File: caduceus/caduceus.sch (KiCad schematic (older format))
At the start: 47 parts

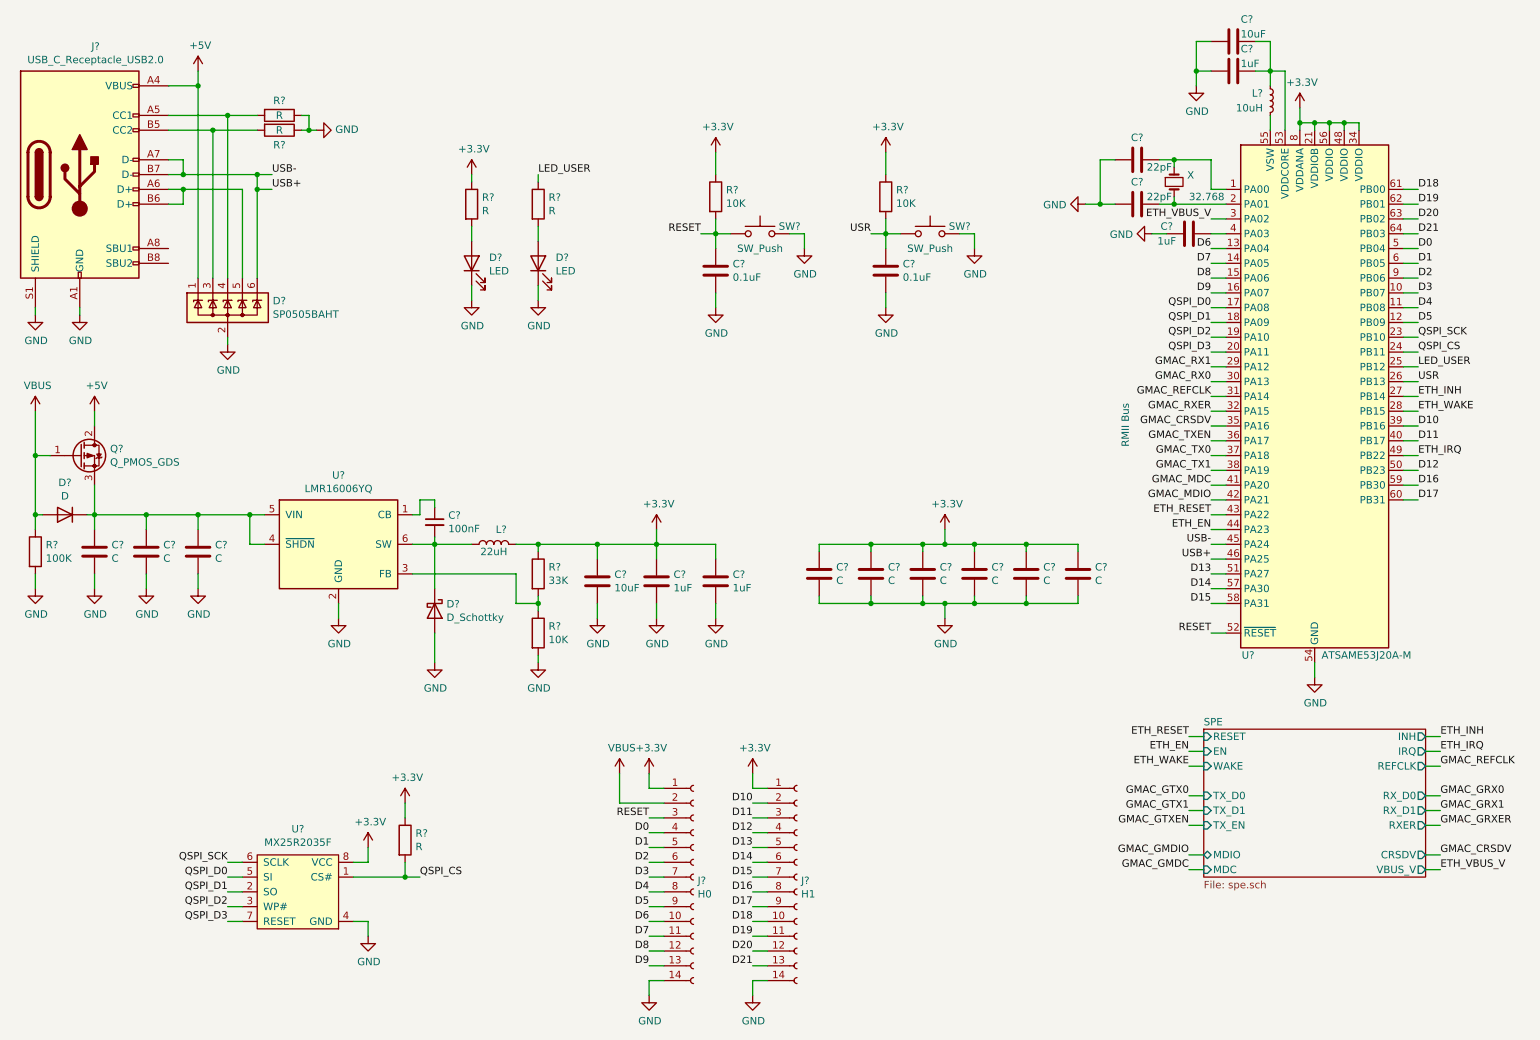
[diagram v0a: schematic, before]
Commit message: Footprints done, not all are final
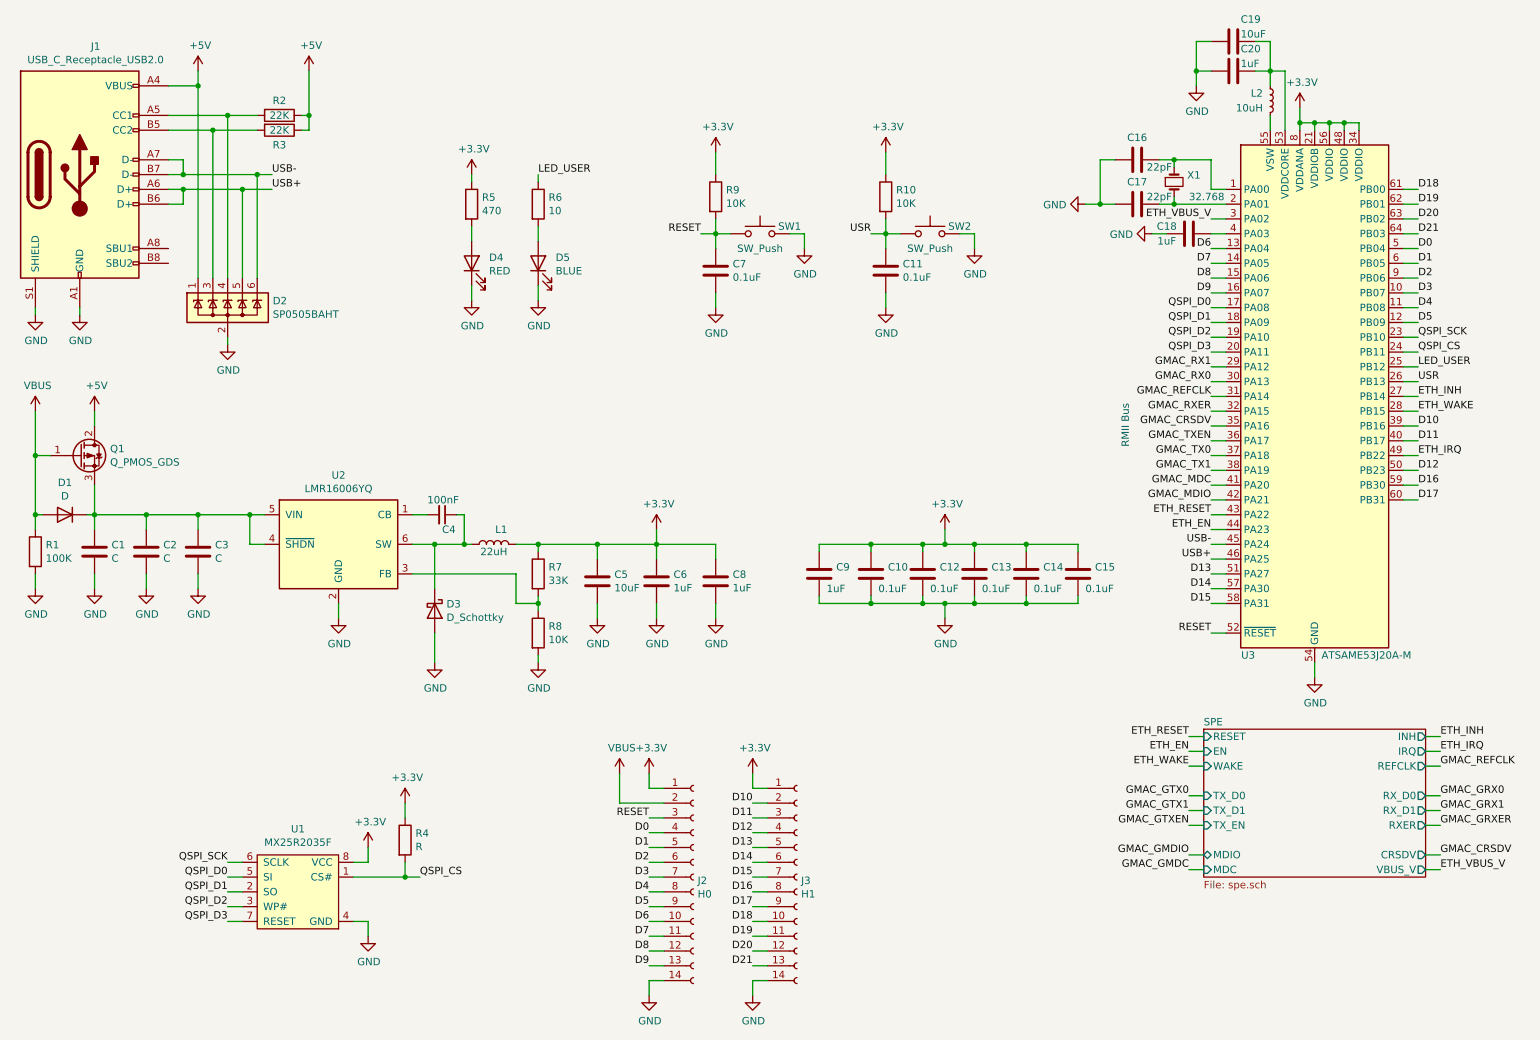
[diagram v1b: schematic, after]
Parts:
- C1, C11, C16, C17, C18, C19, C2, C20, C3, C4, C5, C6, C7, C8: renamed from C?; footprint (none) -> Capacitor_SMD:C_0603_1608Metric
- C10, C12, C13, C14, C15: renamed from C?; value C -> 0.1uF; footprint (none) -> Capacitor_SMD:C_0603_1608Metric
- C9: renamed from C?; value C -> 1uF; footprint (none) -> Capacitor_SMD:C_0603_1608Metric
- D4: renamed from D?; value LED -> RED; PN (none) -> LTST-C171KRKT
- D5: renamed from D?; value LED -> BLUE; PN (none) -> LTST-C171TBKT
- J1: renamed from J?; footprint (none) -> Connector_USB:USB_C_Receptacle_Amphenol_12401610E4-2A_CircularHoles
- J2: renamed from J?; footprint (none) -> Connector_PinHeader_2.54mm:PinHeader_1x10_P2.54mm_Vertical
- J3: renamed from J?; footprint (none) -> Button_Switch_SMD:SW_SPST_B3U-1000P
- R1, R10, R4, R7, R8, R9: renamed from R?; footprint (none) -> Resistor_SMD:R_0603_1608Metric
- R2, R3: renamed from R?; value R -> 22K; footprint (none) -> Resistor_SMD:R_0603_1608Metric
- R5: renamed from R?; value R -> 470; footprint (none) -> Resistor_SMD:R_0603_1608Metric
- R6: renamed from R?; value R -> 10; footprint (none) -> Resistor_SMD:R_0603_1608Metric
- SW1, SW2: renamed from SW?; footprint (none) -> Button_Switch_SMD:SW_SPST_B3U-1000P
- U1: renamed from U?; footprint (none) -> Package_SO:SOP-8_3.9x4.9mm_P1.27mm
- gave numbers to parts that had none: 8
- renumbered X to X1
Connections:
- net +5V: now also R2.1, R3.1
- net GND: no longer R2.1, R3.1
- net USB+: now also D2.5 (K), J1.A6 (D+), J1.B6 (D+); no longer D2.6 (K), J1.A7 (D-), J1.B7 (D-), U3.45 (PA24)
- net at D3.1 (K), L1.1, U2.6 (SW): now also C4.1; no longer C4.2
- net at U2.1 (CB): now also C4.2; no longer C4.1
- new net USB-: D2.6 (K), J1.A7 (D-), J1.B7 (D-), U3.45 (PA24)
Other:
- moved on the sheet: C4

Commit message: Changed PHY IC to DP83TD510E
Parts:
- D1, D3: footprint (none) -> Diode_SMD:D_SOD-123
- D4, D5: footprint (none) -> LED_SMD:LED_0805_2012Metric
- J2: footprint Connector_PinHeader_2.54mm:PinHeader_1x10_P2.54mm_Vertical -> Connector_PinHeader_2.54mm:PinHeader_1x14_P2.54mm_Vertical
- J3: footprint Button_Switch_SMD:SW_SPST_B3U-1000P -> Connector_PinHeader_2.54mm:PinHeader_1x14_P2.54mm_Vertical
- L1: footprint (none) -> Inductor_SMD:L_Coilcraft_XxL4020
- L2: footprint (none) -> Inductor_SMD:L_0805_2012Metric
- Q1: footprint (none) -> Package_TO_SOT_SMD:SOT-23
- SW2: footprint Button_Switch_SMD:SW_SPST_B3U-1000P -> Button_Switch_SMD:SW_SPST_B3U-1000P
- X1: footprint (none) -> Crystal:Crystal_SMD_TXC_9HT11-2Pin_2.0x1.2mm
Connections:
- net D0: now also J2.13 (Pin_13); no longer J2.4 (Pin_4)
- net D1: now also J2.12 (Pin_12); no longer J2.5 (Pin_5)
- net D2: now also J2.11 (Pin_11); no longer J2.6 (Pin_6)
- net D3: now also J2.10 (Pin_10); no longer J2.7 (Pin_7)
- net D4: now also J2.9 (Pin_9); no longer J2.8 (Pin_8)
- net D5: now also J2.8 (Pin_8); no longer J2.9 (Pin_9)
- net D6: now also J2.7 (Pin_7); no longer J2.10 (Pin_10)
- net D7: now also J2.6 (Pin_6); no longer J2.11 (Pin_11)
- net D8: now also J2.5 (Pin_5); no longer J2.12 (Pin_12)
- net D9: now also J2.4 (Pin_4); no longer J2.13 (Pin_13)
- net ETH_INH: no longer names the net of U3.27 (PB14)
- net GMAC_CRSDV renamed G_RDV
- net GMAC_MDC renamed G_MDC
- net GMAC_MDIO renamed G_MDIO
- net GMAC_REFCLK renamed G_REFCLK
- net GMAC_RX0 renamed G_RX0
- net GMAC_RX1 renamed G_RX1
- net GMAC_RXER renamed G_RXER
- net GMAC_TX0 renamed G_TX0
- net GMAC_TX1 renamed G_TX1
- net GMAC_TXEN renamed G_TXEN
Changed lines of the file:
@@
 F 0 "L2" H 9250 1200 50  0000 R CNN
 F 1 "10uH" H 9250 1100 50  0000 R CNN
-F 2 "" H 9300 1150 50  0001 C CNN
+F 2 "Inductor_SMD:L_0805_2012Metric" H 9300 1150 50  0001 C CNN
 F 3 "~" H 9300 1150 50  0001 C CNN
 	1    9300 1150
@@
 F 0 "X1" V 8604 1788 50  0000 L CNN
 F 1 "32.768" V 8750 1800 50  0000 L CNN
-F 2 "" H 8650 1700 50  0001 C CNN
+F 2 "Crystal:Crystal_SMD_TXC_9HT11-2Pin_2.0x1.2mm" H 8650 1700 50  0001 C CNN
 F 3 "~" H 8650 1700 50  0001 C CNN
 	1    8650 1700
@@
 $EndComp
 Text Label 8900 3750 2    50   ~ 0
-GMAC_MDC
+G_MDC
 Wire Wire Line
 	8900 2950 9000 2950
-Text Label 8900 2950 2    50   ~ 0
-GMAC_RX1
 Wire Wire Line
 	8900 3050 9000 3050
-Text Label 8900 3050 2    50   ~ 0
-GMAC_RX0
 Wire Wire Line
 	9000 3150 8900 3150
-Text Label 8900 3150 2    50   ~ 0
-GMAC_REFCLK
 Wire Wire Line
 	8900 3250 9000 3250
-Text Label 8900 3250 2    50   ~ 0
-GMAC_RXER
 Wire Wire Line
 	9000 3350 8900 3350
-Text Label 8900 3350 2    50   ~ 0
-GMAC_CRSDV
 Text Label 8900 3450 2    50   ~ 0
-GMAC_TXEN
+G_TXEN
 Wire Wire Line
 	8900 3450 9000 3450
@@
 	8900 3550 9000 3550
 Text Label 8900 3550 2    50   ~ 0
-GMAC_TX0
+G_TX0
 Text Label 8900 3650 2    50   ~ 0
-GMAC_TX1
+G_TX1
 Wire Wire Line
 	8900 3650 9000 3650
@@
 	0    1    1    0
 $EndComp
-Wire Wire Line
-	8750 6350 8850 6350
-Wire Wire Line
-	8750 6250 8850 6250
-Wire Wire Line
-	8750 6050 8850 6050
 Text Label 8900 3850 2    50   ~ 0
-GMAC_MDIO
-Text Label 8750 6250 2    50   ~ 0
-GMAC_GMDIO
-Text Label 8750 6350 2    50   ~ 0
-GMAC_GMDC
-Text Label 8750 5850 2    50   ~ 0
-GMAC_GTX0
-Wire Wire Line
-	8750 5850 8850 5850
-Text Label 8750 5950 2    50   ~ 0
-GMAC_GTX1
-Wire Wire Line
-	8750 5950 8850 5950
-Text Label 8750 6050 2    50   ~ 0
-GMAC_GTXEN
-Text Label 10450 5950 0    50   ~ 0
-GMAC_GRX1
-Wire Wire Line
-	10450 5950 10350 5950
-Text Label 10450 5850 0    50   ~ 0
-GMAC_GRX0
-Wire Wire Line
-	10450 5850 10350 5850
-Text Label 10450 6050 0    50   ~ 0
-GMAC_GRXER
-Wire Wire Line
-	10450 6050 10350 6050
-Text Label 10450 6250 0    50   ~ 0
-GMAC_CRSDV
-Wire Wire Line
-	10350 6250 10450 6250
-Text Label 10450 5650 0    50   ~ 0
-GMAC_REFCLK
-Wire Wire Line
-	10450 5650 10350 5650
+G_MDIO
 Wire Wire Line
 	9000 3950 8900 3950
@@
 Wire Wire Line
 	8900 4150 9000 4150
-Wire Wire Line
-	8750 5650 8850 5650
-Wire Wire Line
-	8750 5550 8850 5550
-Wire Wire Line
-	8750 5450 8850 5450
-Wire Wire Line
-	10450 5450 10350 5450
-Wire Wire Line
-	10450 5550 10350 5550
-Text Label 10450 5550 0    50   ~ 0
-ETH_IRQ
-Text Label 10450 5450 0    50   ~ 0
-ETH_INH
-Text Label 8750 5450 2    50   ~ 0
-ETH_RESET
-Text Label 8750 5550 2    50   ~ 0
-ETH_EN
-Text Label 8750 5650 2    50   ~ 0
-ETH_WAKE
 Text Label 8900 3950 2    50   ~ 0
 ETH_RESET
@@
 Text Label 10300 3250 0    50   ~ 0
 ETH_WAKE
-Text Label 10300 3150 0    50   ~ 0
-ETH_INH
 Wire Wire Line
 	10200 3550 10300 3550
@@
 Wire Wire Line
 	10300 3250 10200 3250
-Wire Wire Line
-	10300 3150 10200 3150
 $Comp
 L Connector:USB_C_Receptacle_USB2.0 J1
@@
 F 0 "Q1" H 1455 3596 50  0000 L CNN
 F 1 "Q_PMOS_GDS" H 1455 3505 50  0000 L CNN
-F 2 "" H 1450 3650 50  0001 C CNN
+F 2 "Package_TO_SOT_SMD:SOT-23" H 1450 3650 50  0001 C CNN
 F 3 "~" H 1250 3550 50  0001 C CNN
 	1    1250 3550
@@
 F 0 "D1" H 1150 3733 50  0000 C CNN
 F 1 "D" H 1150 3824 50  0000 C CNN
-F 2 "" H 1150 3950 50  0001 C CNN
+F 2 "Diode_SMD:D_SOD-123" H 1150 3950 50  0001 C CNN
 F 3 "~" H 1150 3950 50  0001 C CNN
 	1    1150 3950
@@
 F 0 "L1" V 4150 4100 50  0000 C CNN
 F 1 "22uH" V 4000 4150 50  0000 C CNN
-F 2 "" H 4050 4150 50  0001 C CNN
+F 2 "Inductor_SMD:L_Coilcraft_XxL4020" H 4050 4150 50  0001 C CNN
 F 3 "~" H 4050 4150 50  0001 C CNN
 	1    4050 4150
@@
 F 0 "D3" V 3604 4680 50  0000 L CNN
 F 1 "D_Schottky" V 3695 4680 50  0000 L CNN
-F 2 "" H 3650 4600 50  0001 C CNN
+F 2 "Diode_SMD:D_SOD-123" H 3650 4600 50  0001 C CNN
 F 3 "~" H 3650 4600 50  0001 C CNN
 	1    3650 4600
@@
 	1    0    0    -1
 $EndComp
-$Sheet
-S 8850 5400 1500 1000
-U 5F963ECA
-F0 "SPE" 50
-F1 "spe.sch" 50
-F2 "TX_D1" I L 8850 5950 50
-F3 "TX_D0" I L 8850 5850 50
-F4 "REFCLK" O R 10350 5650 50
-F5 "CRSDV" O R 10350 6250 50
-F6 "TX_EN" I L 8850 6050 50
-F7 "RXER" O R 10350 6050 50
-F8 "MDC" I L 8850 6350 50
-F9 "MDIO" B L 8850 6250 50
-F10 "RX_D1" O R 10350 5950 50
-F11 "RX_D0" O R 10350 5850 50
-F12 "EN" I L 8850 5550 50
-F13 "RESET" I L 8850 5450 50
-F14 "WAKE" I L 8850 5650 50
-F15 "IRQ" O R 10350 5550 50
-F16 "INH" O R 10350 5450 50
-F17 "VBUS_V" O R 10350 6350 50
-$EndSheet
-Wire Wire Line
-	10450 6350 10350 6350
-Text Label 10450 6350 0    50   ~ 0
-ETH_VBUS_V
 Wire Wire Line
 	9000 1950 8900 1950
@@
 Wire Wire Line
 	5100 7100 5100 7200
-Text Label 5100 6200 2    50   ~ 0
+Text Label 5100 6900 2    50   ~ 0
 D1
-Text Label 5100 6100 2    50   ~ 0
+Text Label 5100 7000 2    50   ~ 0
 D0
 $Comp
@@
 $EndComp
 Wire Wire Line
+	5100 7000 5200 7000
+Wire Wire Line
+	5100 6900 5200 6900
+Wire Wire Line
+	5100 6800 5200 6800
+Wire Wire Line
+	5100 6700 5200 6700
+Wire Wire Line
+	5100 6600 5200 6600
+Wire Wire Line
+	5100 6500 5200 6500
+Wire Wire Line
+	5100 6400 5200 6400
+Wire Wire Line
+	5100 6300 5200 6300
+Wire Wire Line
+	5100 6200 5200 6200
+Wire Wire Line
 	5100 6100 5200 6100
-Wire Wire Line
-	5100 6200 5200 6200
-Wire Wire Line
-	5100 6300 5200 6300
-Wire Wire Line
-	5100 6400 5200 6400
-Wire Wire Line
-	5100 6500 5200 6500
-Wire Wire Line
-	5100 6600 5200 6600
-Wire Wire Line
-	5100 6700 5200 6700
-Wire Wire Line
-	5100 6800 5200 6800
-Wire Wire Line
-	5100 6900 5200 6900
-Wire Wire Line
-	5100 7000 5200 7000
 Wire Wire Line
 	5900 7100 5800 7100
@@
 Text Label 8900 2450 2    50   ~ 0
 D9
+Text Label 5100 6800 2    50   ~ 0
+D2
+Text Label 5100 6700 2    50   ~ 0
+D3
+Text Label 5100 6600 2    50   ~ 0
+D4
+Text Label 5100 6500 2    50   ~ 0
+D5
+Text Label 5100 6400 2    50   ~ 0
+D6
 Text Label 5100 6300 2    50   ~ 0
-D2
-Text Label 5100 6400 2    50   ~ 0
-D3
-Text Label 5100 6500 2    50   ~ 0
-D4
-Text Label 5100 6600 2    50   ~ 0
-D5
-Text Label 5100 6700 2    50   ~ 0
-D6
-Text Label 5100 6800 2    50   ~ 0
 D7
-Text Label 5100 6900 2    50   ~ 0
+Text Label 5100 6200 2    50   ~ 0
 D8
-Text Label 5100 7000 2    50   ~ 0
+Text Label 5100 6100 2    50   ~ 0
 D9
 Text Label 10300 3350 0    50   ~ 0
@@
 F 0 "J2" H 5428 6376 50  0000 L CNN
 F 1 "H0" H 5428 6285 50  0000 L CNN
-F 2 "Connector_PinHeader_2.54mm:PinHeader_1x10_P2.54mm_Vertical" H 5400 6400 50  0001 C CNN
+F 2 "Connector_PinHeader_2.54mm:PinHeader_1x14_P2.54mm_Vertical" H 5400 6400 50  0001 C CNN
 F 3 "~" H 5400 6400 50  0001 C CNN
 	1    5400 6400
@@
 F 0 "J3" H 6128 6376 50  0000 L CNN
 F 1 "H1" H 6128 6285 50  0000 L CNN
-F 2 "Button_Switch_SMD:SW_SPST_B3U-1000P" H 6100 6400 50  0001 C CNN
+F 2 "Connector_PinHeader_2.54mm:PinHeader_1x14_P2.54mm_Vertical" H 6100 6400 50  0001 C CNN
 F 3 "~" H 6100 6400 50  0001 C CNN
 	1    6100 6400
@@
 F 0 "SW2" H 7200 2100 50  0000 C CNN
 F 1 "SW_Push" H 7000 1950 50  0000 C CNN
-F 2 " Button_Switch_SMD:SW_SPST_B3U-1000P" H 7000 2250 50  0001 C CNN
+F 2 "Button_Switch_SMD:SW_SPST_B3U-1000P" H 7000 2250 50  0001 C CNN
 F 3 "~" H 7000 2250 50  0001 C CNN
 	1    7000 2050
@@
 F 0 "D5" V 4389 2132 50  0000 R CNN
 F 1 "BLUE" V 4298 2132 50  0000 R CNN
-F 2 "" H 4350 2250 50  0001 C CNN
+F 2 "LED_SMD:LED_0805_2012Metric" H 4350 2250 50  0001 C CNN
 F 3 "~" H 4350 2250 50  0001 C CNN
 F 4 "LTST-C171TBKT" V 4350 2250 50  0001 C CNN "PN"
@@
 F 0 "D4" V 3939 2132 50  0000 R CNN
 F 1 "RED" V 3848 2132 50  0000 R CNN
-F 2 "" H 3900 2250 50  0001 C CNN
+F 2 "LED_SMD:LED_0805_2012Metric" H 3900 2250 50  0001 C CNN
 F 3 "~" H 3900 2250 50  0001 C CNN
 F 4 "LTST-C171KRKT" V 3900 2250 50  0001 C CNN "PN"
@@
 	0    -1   -1   0
 $EndComp
+$Sheet
+S 8850 5400 1500 1000
+U 5F963ECA
+F0 "SPE" 50
+F1 "spe.sch" 50
+F2 "VBUS_V" O R 10350 5450 50
+F3 "MDIO" B L 8850 6250 50
+F4 "MDC" I L 8850 6350 50
+F5 "TX_D0" I L 8850 5900 50
+F6 "TX_D1" I L 8850 6000 50
+F7 "RX_D0" O R 10350 5900 50
+F8 "RX_D1" O R 10350 6000 50
+F9 "TX_EN" I L 8850 5800 50
+F10 "RX_ERR" O R 10350 5800 50
+F11 "RX_DV" O R 10350 5700 50
+F12 "TX_CLK" I L 8850 5700 50
+F13 "PWRD" O R 10350 6150 50
+F14 "RESET" I L 8850 5450 50
+$EndSheet
+Text Label 8900 2950 2    50   ~ 0
+G_RX1
+Text Label 10450 6000 0    50   ~ 0
+G_RX1
+Text Label 10450 5900 0    50   ~ 0
+G_RX0
+Wire Wire Line
+	10450 5900 10350 5900
+Wire Wire Line
+	10350 6000 10450 6000
+Text Label 8900 3050 2    50   ~ 0
+G_RX0
+Text Label 8900 3150 2    50   ~ 0
+G_REFCLK
+Text Label 8900 3250 2    50   ~ 0
+G_RXER
+Text Label 8900 3350 2    50   ~ 0
+G_RDV
+Text Label 10450 5700 0    50   ~ 0
+G_RDV
+Wire Wire Line
+	10450 5700 10350 5700
+Text Label 8750 6250 2    50   ~ 0
+G_MDIO
+Wire Wire Line
+	8750 6250 8850 6250
+Text Label 8750 6350 2    50   ~ 0
+G_MDC
+Wire Wire Line
+	8750 6350 8850 6350
+Text Label 8750 5900 2    50   ~ 0
+G_TX0
+Wire Wire Line
+	8750 5900 8850 5900
+Text Label 8750 6000 2    50   ~ 0
+G_TX1
+Wire Wire Line
+	8750 6000 8850 6000
+Text Label 8750 5450 2    50   ~ 0
+ETH_RESET
+Wire Wire Line
+	8750 5450 8850 5450
+Text Label 10450 5800 0    50   ~ 0
+G_RXER
+Wire Wire Line
+	10450 5800 10350 5800
+Text Label 10450 6150 0    50   ~ 0
+ETH_WAKE
+Wire Wire Line
+	10450 6150 10350 6150
+Text Label 8750 5800 2    50   ~ 0
+G_TXEN
+Text Label 8750 5700 2    50   ~ 0
+G_REFCLK
+Wire Wire Line
+	8750 5700 8850 5700
+Wire Wire Line
+	8750 5800 8850 5800
 $EndSCHEMATC
